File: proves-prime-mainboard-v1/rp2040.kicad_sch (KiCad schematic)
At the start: 30 parts, among them IC1 RP2040_QFN56, IC2 AZ1117CH-3.3TRG1, U1 W25Q128JV, Y1 12MHZ

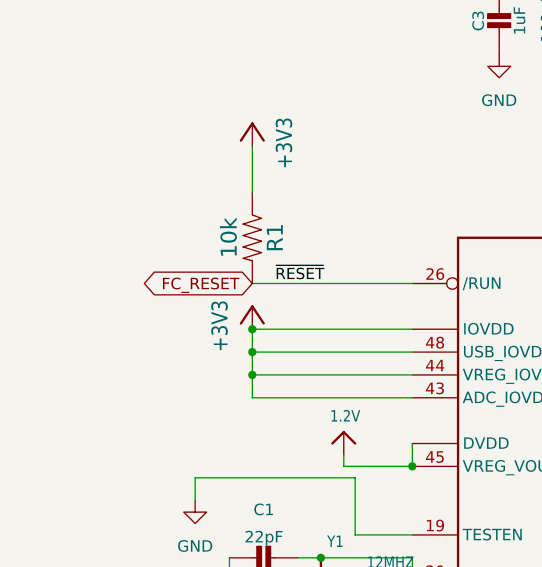
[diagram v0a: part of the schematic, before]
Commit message: Copied Watchdog Circuit
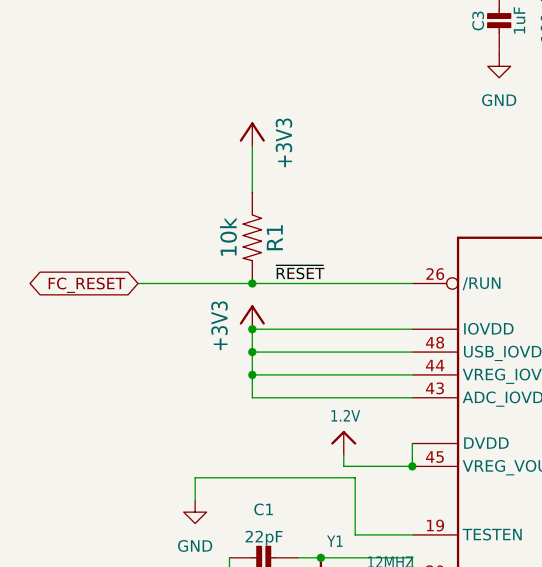
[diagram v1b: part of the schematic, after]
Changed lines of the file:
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@@
+	)
+	(junction
+		(at 62.23 64.77)
+		(diameter 0)
+		(color 0 0 0 0)
 	)
 	(junction
@@
 	(wire
 		(pts
+			(xy 49.53 64.77) (xy 62.23 64.77)
+		)
+		(stroke
+			(width 0)
+			(type default)
+		)
+	)
+	(wire
+		(pts
 			(xy 200.66 48.26) (xy 219.71 48.26)
 		)
@@
 	(global_label "FC_RESET"
 		(shape bidirectional)
-		(at 62.23 64.77 180)
+		(at 49.53 64.77 180)
 		(fields_autoplaced yes)
 		(effects
@@
 		)
 		(property "Intersheetrefs" "${INTERSHEET_REFS}"
-			(at 49.1416 64.77 0)
-			(effects
-				(font
+			(at 36.4416 64.77 0)
+			(effects
+				(font

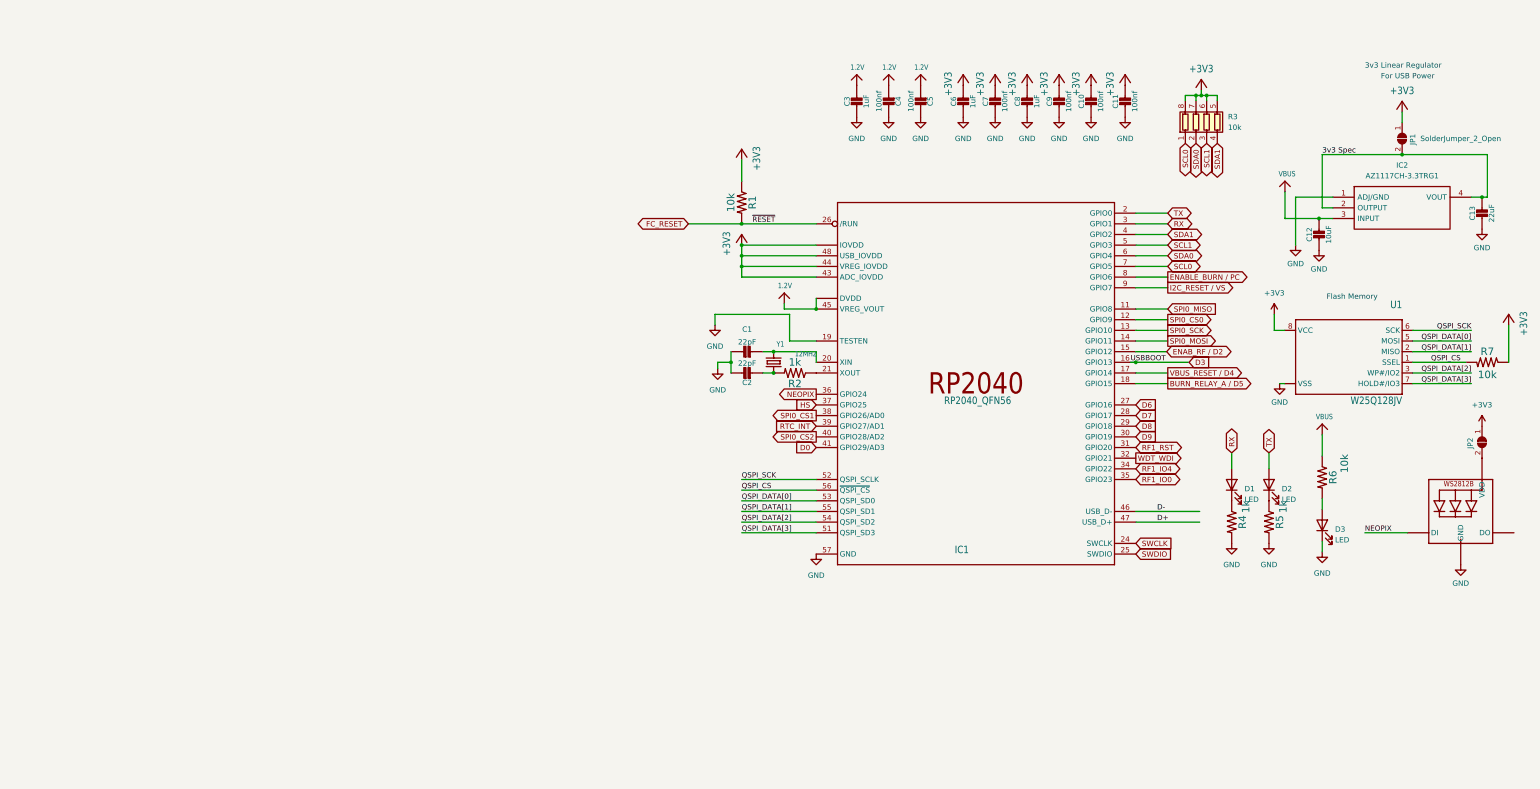
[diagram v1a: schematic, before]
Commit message: Migrated FC Board Elements
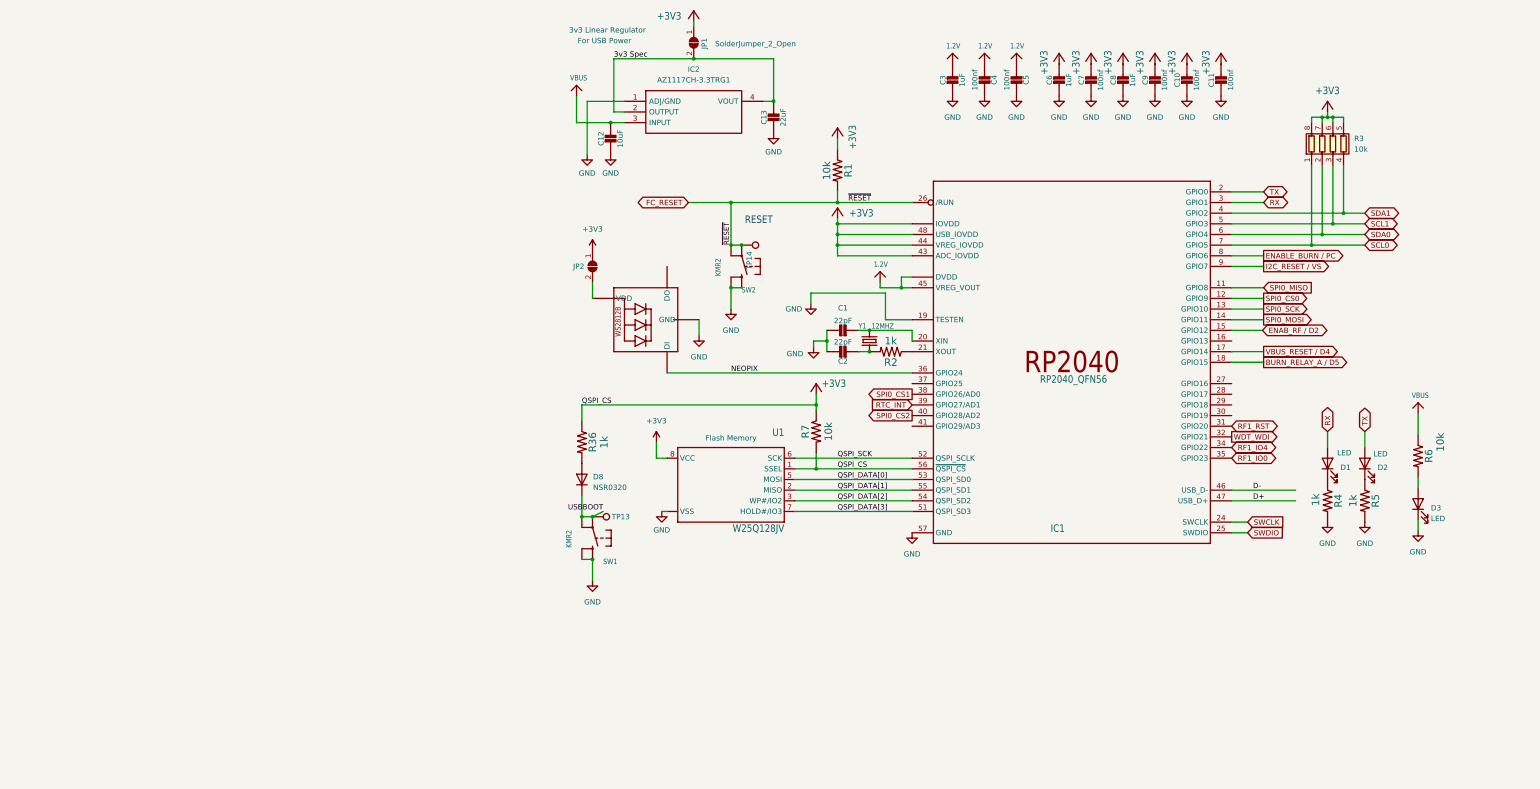
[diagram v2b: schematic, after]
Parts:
- added D8: NSR0320, Diode_SMD:D_SOD-323F, symbol Diode:1SS355VM
- added R36: 1k, Resistor_SMD:R_0603_1608Metric, symbol mainboard:RESISTOR0603
- added SW1, SW2: KMR2, FC_DEV_BOARD:BTN_KMR2_4.6X2.8, symbol Adafruit ItsyBitsy RP2040-eagle-import:SWITCH_TACT_SMT4.6X2.8
- added TP13: USBBOOT, TestPoint:TestPoint_Loop_D1.80mm_Drill1.0mm_Beaded, symbol Connector:TestPoint
- added TP14: RESET, TestPoint:TestPoint_Loop_D1.80mm_Drill1.0mm_Beaded, symbol Connector:TestPoint
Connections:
- net QSPI_CS is gone; now on net +3V3: IC1.56 (~{QSPI_CS}), R7.2, U1.1 (SSEL)
- net +3V3: now also R36.1
- net FC_RESET: now also SW2.A (P), SW2.A' (P1), TP14.1
- net GND: now also SW1.B (S), SW1.B' (S1), SW2.B (S), SW2.B' (S1)
- net D0: no longer names the net of IC1.41 (GPIO29/AD3)
- net D3: no longer names the net of IC1.16 (GPIO13)
- net D6: no longer names the net of IC1.27 (GPIO16)
- net D7: no longer names the net of IC1.28 (GPIO17)
- net D8: no longer names the net of IC1.29 (GPIO18)
- net D9: no longer names the net of IC1.30 (GPIO19)
- net HS: no longer names the net of IC1.37 (GPIO25)
- new net: D8.2 (A), R36.2
- new net USBBOOT: D8.1 (K), SW1.A (P), SW1.A' (P1), TP13.1
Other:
- note added: "RESET"
- moved on the sheet: C1, C10, C11, C12, C13, C2, C3, C4, C5, C6, C7, C8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

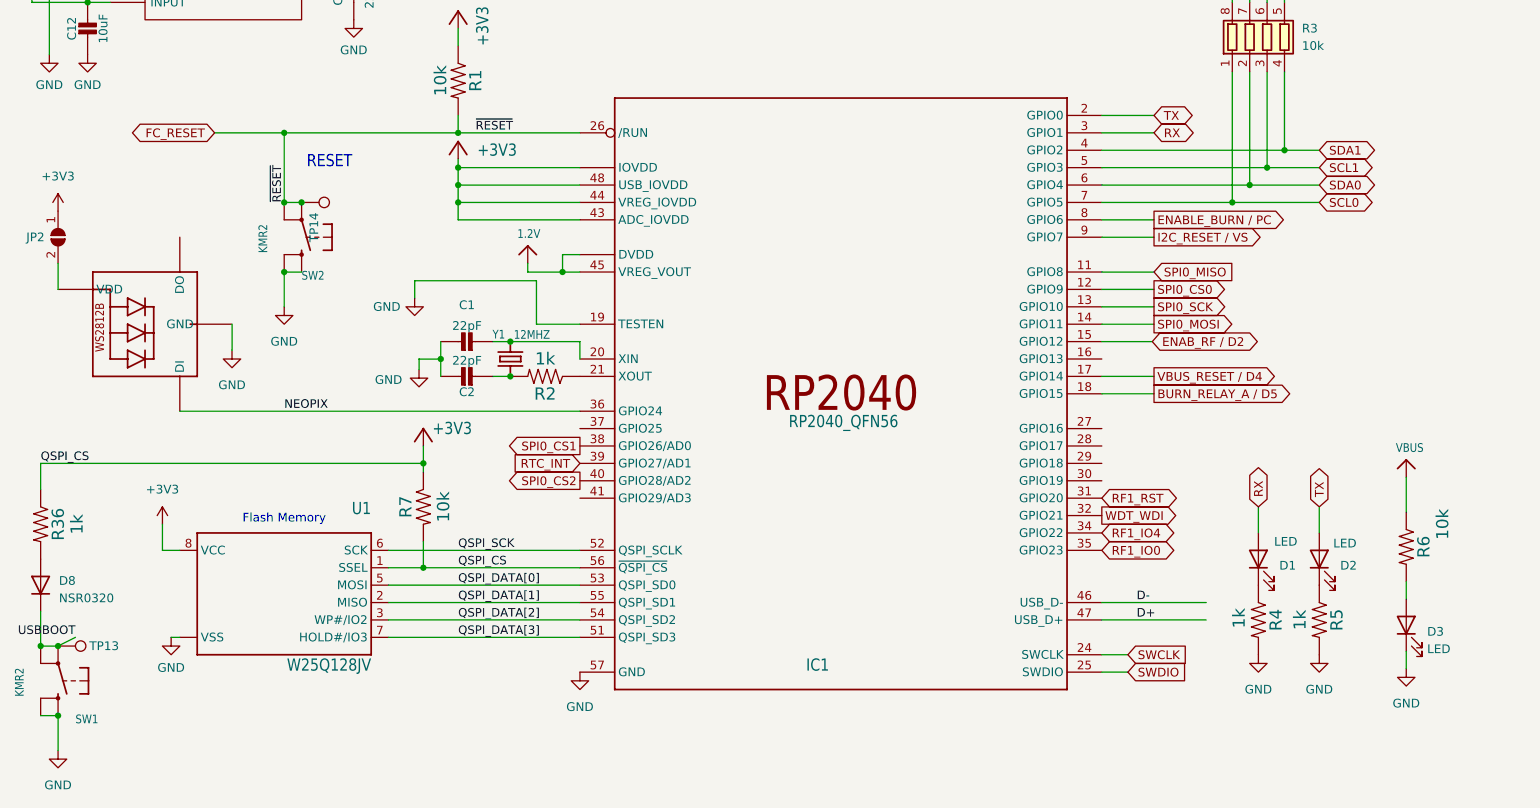
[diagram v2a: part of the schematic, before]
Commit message: Duplicated Radios
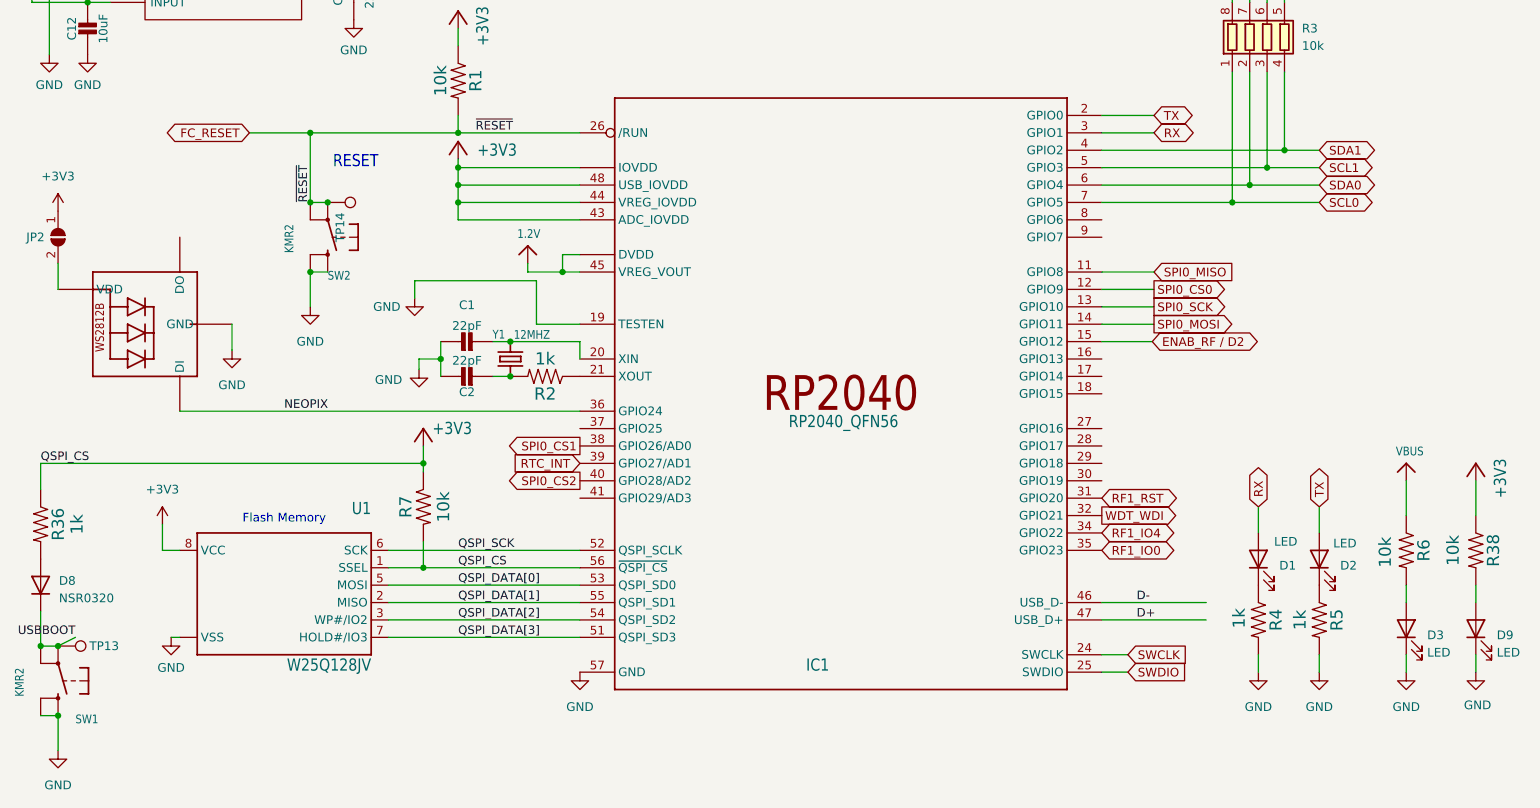
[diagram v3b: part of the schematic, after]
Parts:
- added D9: LED, LED_SMD:LED_0603_1608Metric, symbol Device:LED
- added R38: 10k, Resistor_SMD:R_0603_1608Metric, symbol mainboard:RESISTOR0603
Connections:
- net +3V3: now also R38.1
- net GND: now also D9.1 (K)
- net BURN_RELAY_A / D5: no longer names the net of IC1.18 (GPIO15)
- net ENABLE_BURN / PC: no longer names the net of IC1.8 (GPIO6)
- net I2C_RESET / VS: no longer names the net of IC1.9 (GPIO7)
- net VBUS_RESET / D4: no longer names the net of IC1.17 (GPIO14)
- new net: D9.2 (A), R38.2
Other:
- moved on the sheet: D3, R6, SW2, TP14

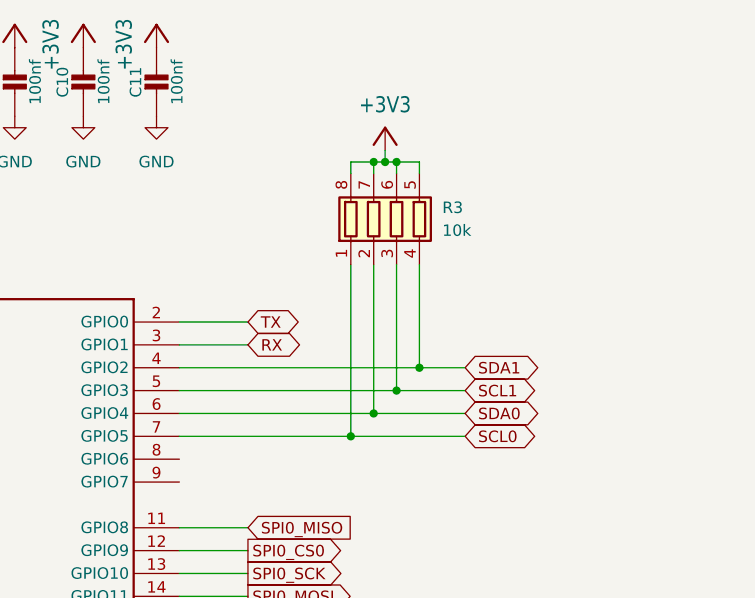
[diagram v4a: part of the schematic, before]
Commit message: Migrated Power Monitor ICs
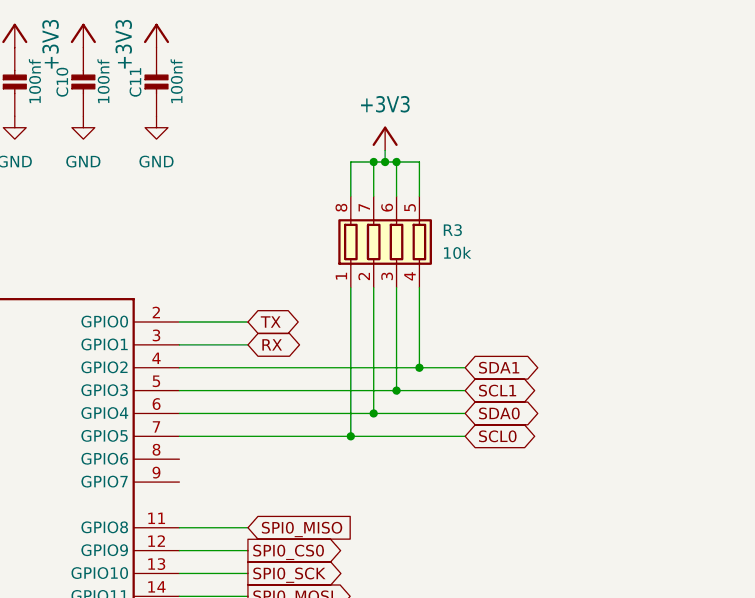
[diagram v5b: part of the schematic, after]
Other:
- moved on the sheet: R3
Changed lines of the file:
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@@
 	(wire
 		(pts
-			(xy 203.2 50.8) (xy 203.2 64.77)
+			(xy 203.2 53.34) (xy 203.2 64.77)
 		)
 		(stroke
@@
 	(wire
 		(pts
-			(xy 200.66 39.37) (xy 200.66 40.64)
+			(xy 200.66 39.37) (xy 200.66 43.18)
 		)
 		(stroke
@@
 	(wire
 		(pts
-			(xy 198.12 50.8) (xy 198.12 69.85)
+			(xy 198.12 53.34) (xy 198.12 69.85)
 		)
 		(stroke
@@
 	(wire
 		(pts
-			(xy 198.12 39.37) (xy 198.12 40.64)
+			(xy 198.12 39.37) (xy 198.12 43.18)
 		)
 		(stroke
@@
 	(wire
 		(pts
-			(xy 203.2 40.64) (xy 203.2 39.37)
+			(xy 203.2 43.18) (xy 203.2 39.37)
 		)
 		(stroke
@@
 	(wire
 		(pts
-			(xy 205.74 50.8) (xy 205.74 62.23)
-		)
-		(stroke
-			(width 0)
-			(type default)
-		)
-	)
-	(wire
-		(pts
-			(xy 205.74 40.64) (xy 205.74 39.37)
+			(xy 205.74 53.34) (xy 205.74 62.23)
+		)
+		(stroke
+			(width 0)
+			(type default)
+		)
+	)
+	(wire
+		(pts
+			(xy 205.74 43.18) (xy 205.74 39.37)
 		)
 		(stroke
@@
 	(wire
 		(pts
-			(xy 200.66 50.8) (xy 200.66 67.31)
+			(xy 200.66 53.34) (xy 200.66 67.31)
 		)
 		(stroke
@@
 	(symbol
 		(lib_id "Device:R_Pack04")
-		(at 203.2 45.72 0)
+		(at 203.2 48.26 0)
 		(unit 1)
 		(exclude_from_sim no)
@@
 		(dnp no)
 		(property "Reference" "R3"
-			(at 208.28 44.4499 0)
+			(at 208.28 46.9899 0)
 			(effects
 				(font
@@
 		)
 		(property "Value" "10k"
-			(at 208.28 46.9899 0)
+			(at 208.28 49.5299 0)
 			(effects
 				(font
@@
 		)
 		(property "Footprint" "Resistor_SMD:R_Array_Convex_4x0603"
-			(at 210.185 45.72 90)
+			(at 210.185 48.26 90)
 			(effects
 				(font
@@
 		)
 		(property "Datasheet" "~"
-			(at 203.2 45.72 0)
+			(at 203.2 48.26 0)
 			(effects
 				(font
@@
 		)
 		(property "Description" ""
-			(at 203.2 45.72 0)
-			(effects
-				(font
+			(at 203.2 48.26 0)
+			(effects
+				(font

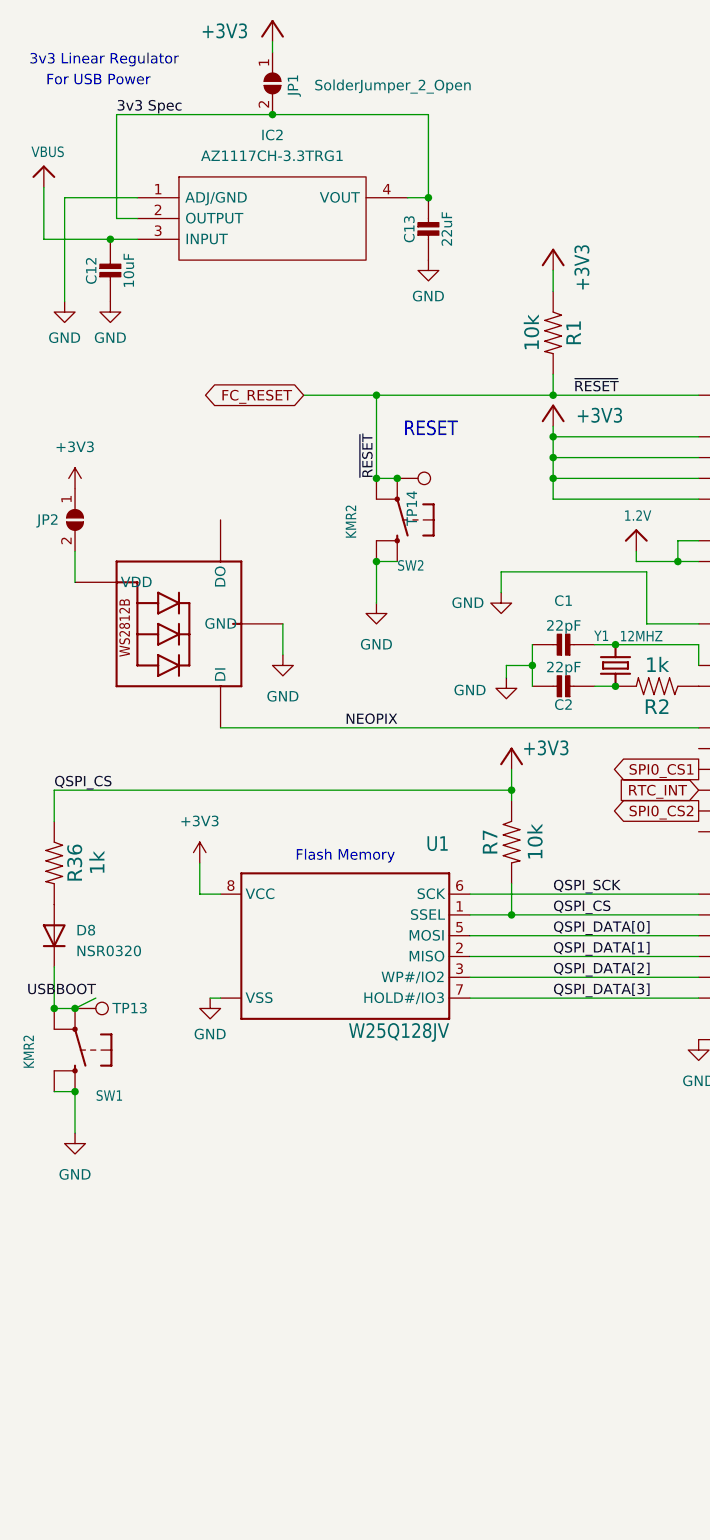
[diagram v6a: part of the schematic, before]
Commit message: Update rp2040.kicad_sch
Added switch for enabling USB 3v3
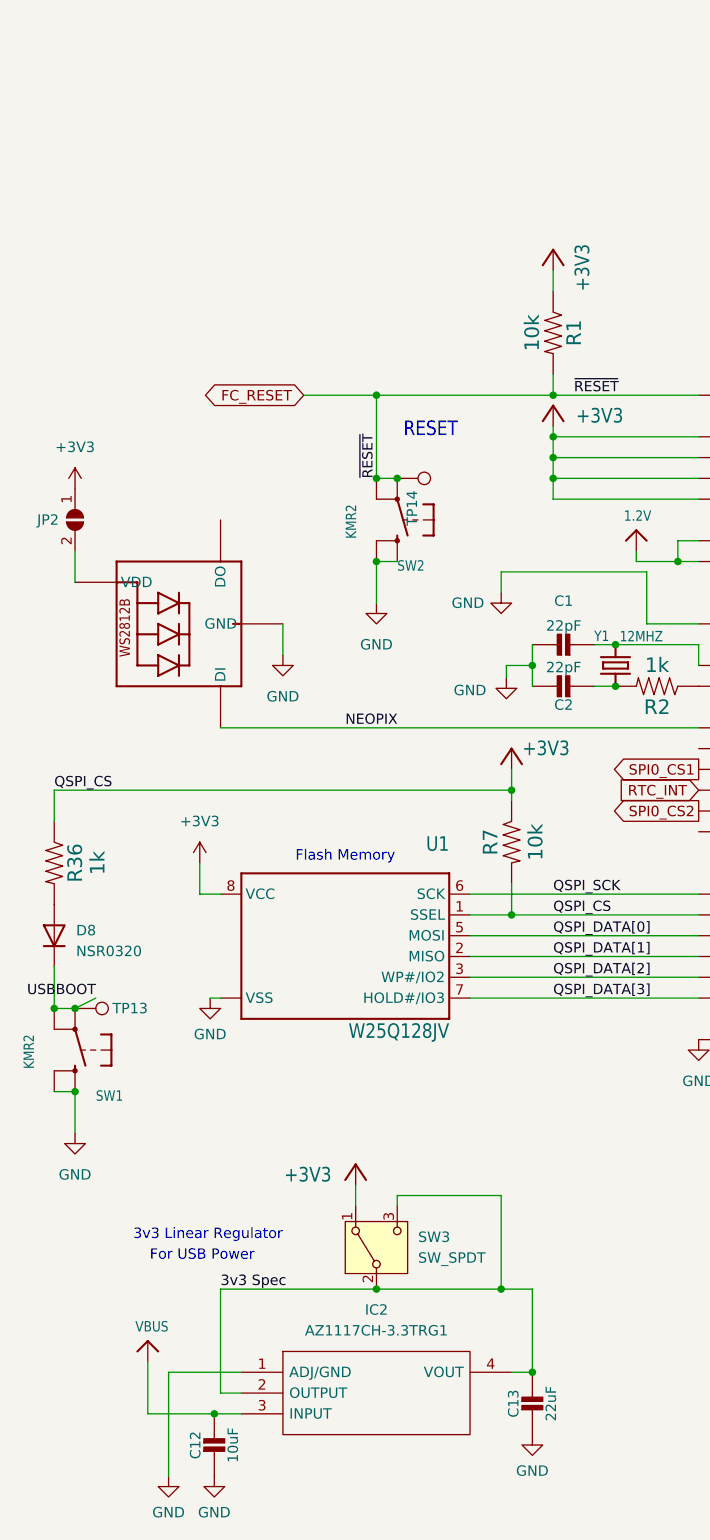
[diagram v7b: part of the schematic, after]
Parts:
- removed JP1: SolderJumper_2_Open, Jumper:SolderJumper-2_P1.3mm_Open_RoundedPad1.0x1.5mm, symbol Jumper:SolderJumper_2_Open
- added SW3: SW_SPDT, symbol Switch:SW_SPDT
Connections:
- net +3V3: now also SW3.1 (A)
- net 3v3 Spec: now also SW3.2 (B), SW3.3 (C)
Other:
- moved on the sheet: C12, C13, IC2
